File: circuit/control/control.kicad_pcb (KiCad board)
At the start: 2 copper layers, 34 parts, among them J1 Conn_01x02_Socket, J2 Conn_02x20_Row_Letter_Last, J3 Conn_02x20_Row_Letter_Last, Q1 2SC1815, Q2 2SC1815, Q3 2SC1815, Q4 2SC1815, Q5 2SC1815, SW1 SW_Push, U1 ESP32-DevKitC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

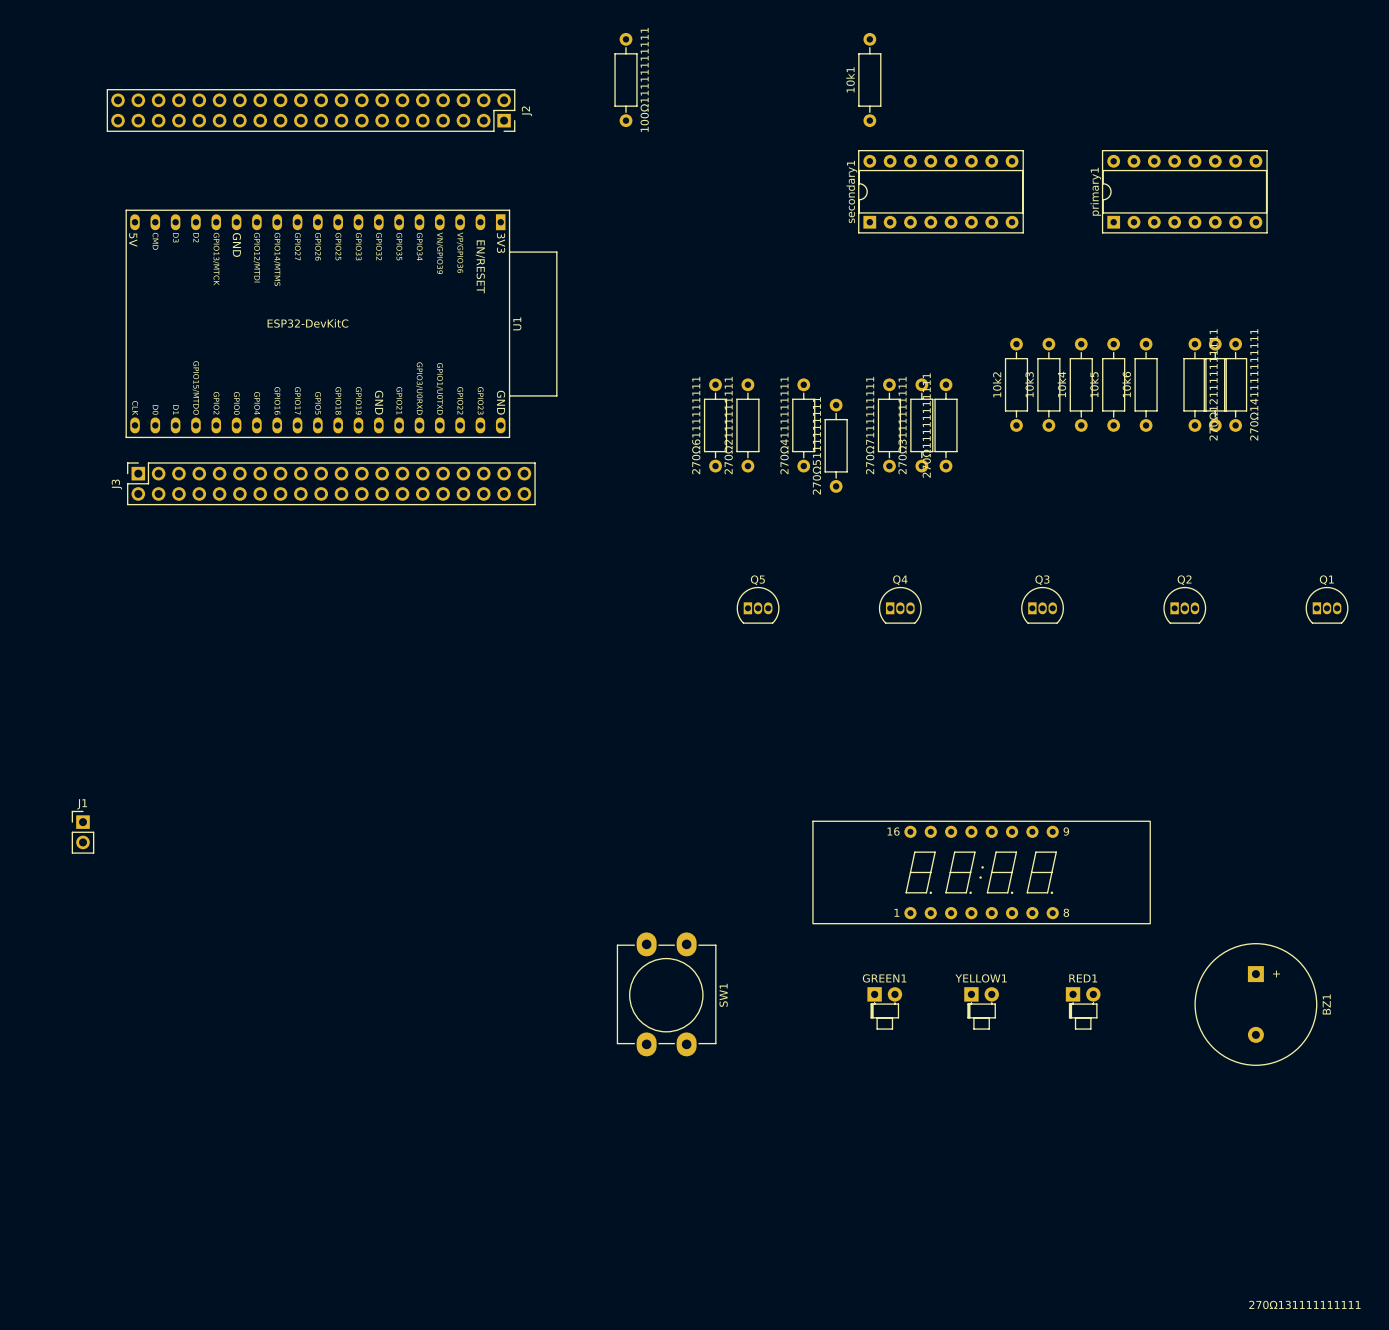
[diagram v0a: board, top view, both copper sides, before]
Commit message: [update] update control circuit
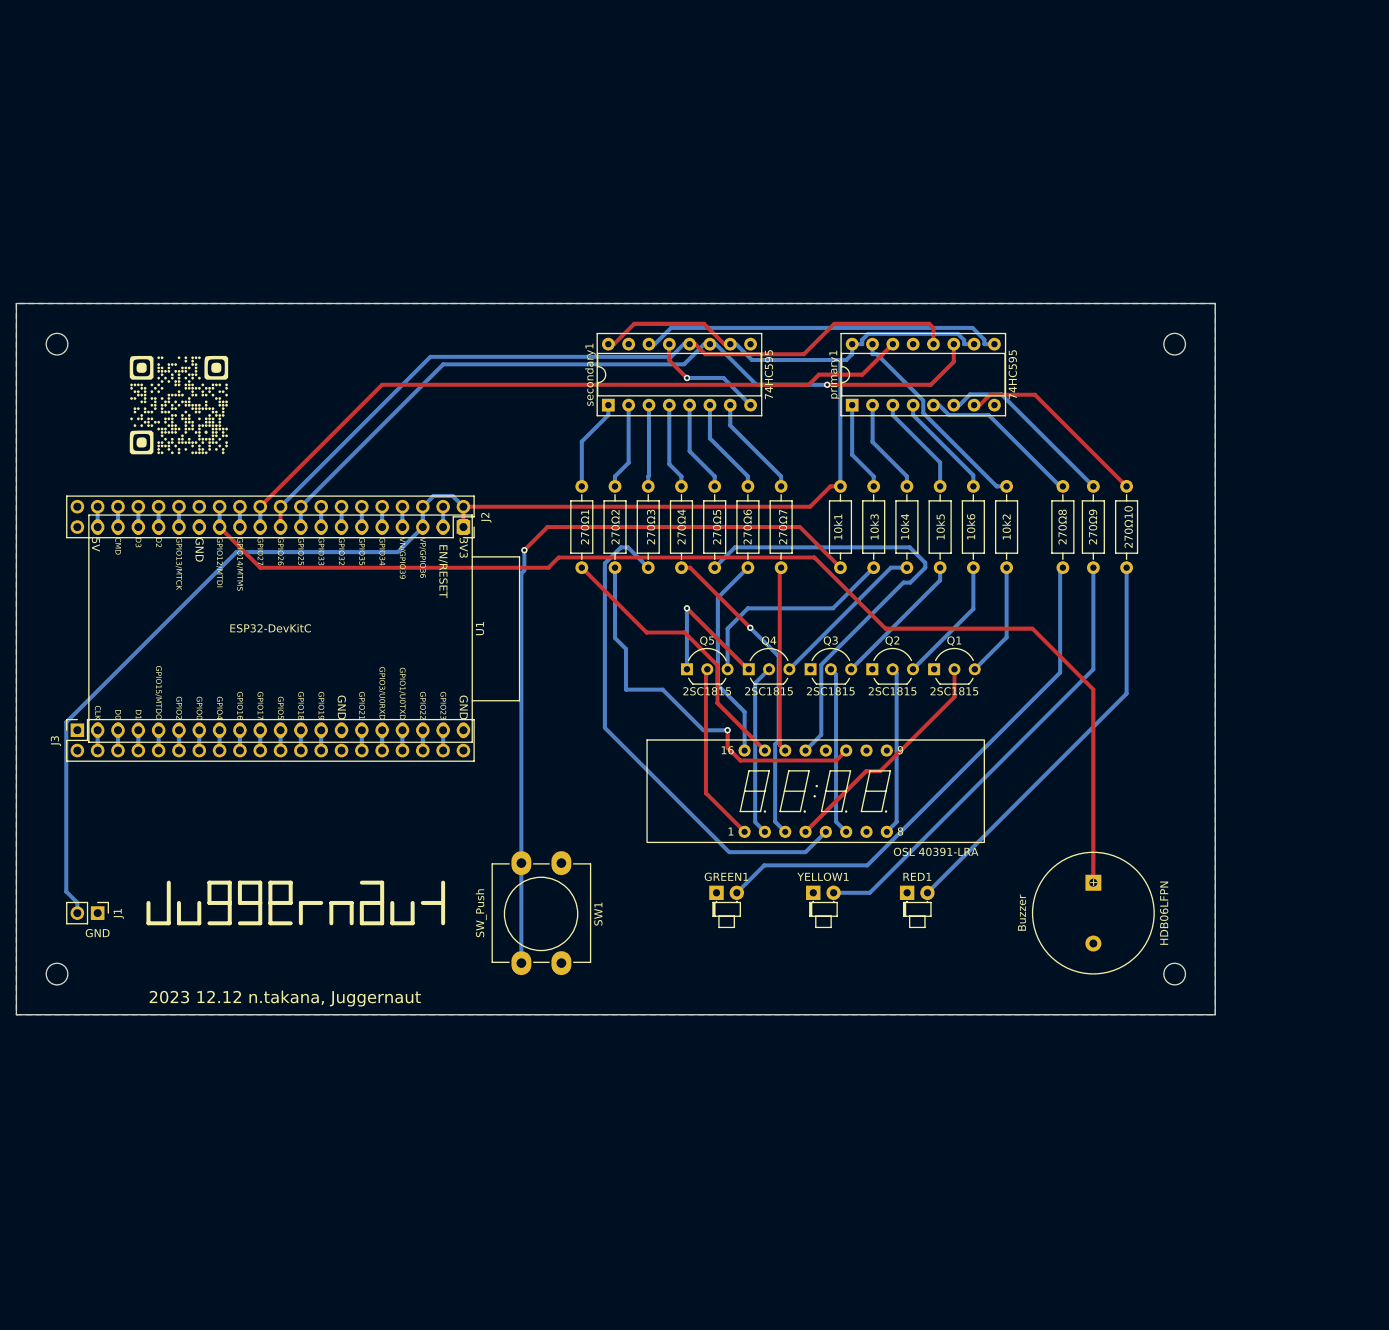
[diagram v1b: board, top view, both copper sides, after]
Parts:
- removed 100Ω11111111111, 270Ω11111111111, 270Ω121111111111, 270Ω131111111111, 270Ω141111111111, 270Ω2111111111, 270Ω3111111111, 270Ω4111111111, 270Ω5111111111, 270Ω6111111111, 270Ω7111111111: R_US, Resistor_THT:R_Axial_DIN0207_L6.3mm_D2.5mm_P10.16mm_Horizontal
- removed BZ1: Buzzer, Buzzer_Beeper:Buzzer_15x7.5RM7.6
- added 270Ω1: R_US, Resistor_THT:R_Axial_DIN0207_L6.3mm_D2.5mm_P10.16mm_Horizontal, F.Cu at (162.1, 96.5)
- added 270Ω10: R_US, Resistor_THT:R_Axial_DIN0207_L6.3mm_D2.5mm_P10.16mm_Horizontal, F.Cu at (230.2, 86.4)
- added 270Ω2: R_US, Resistor_THT:R_Axial_DIN0207_L6.3mm_D2.5mm_P10.16mm_Horizontal, F.Cu at (166.3, 96.5)
- added 270Ω3: R_US, Resistor_THT:R_Axial_DIN0207_L6.3mm_D2.5mm_P10.16mm_Horizontal, F.Cu at (170.4, 96.5)
- added 270Ω4: R_US, Resistor_THT:R_Axial_DIN0207_L6.3mm_D2.5mm_P10.16mm_Horizontal, F.Cu at (174.6, 96.5)
- added 270Ω5: R_US, Resistor_THT:R_Axial_DIN0207_L6.3mm_D2.5mm_P10.16mm_Horizontal, F.Cu at (178.7, 96.5)
- added 270Ω6: R_US, Resistor_THT:R_Axial_DIN0207_L6.3mm_D2.5mm_P10.16mm_Horizontal, F.Cu at (182.9, 96.5)
- added 270Ω7: R_US, Resistor_THT:R_Axial_DIN0207_L6.3mm_D2.5mm_P10.16mm_Horizontal, F.Cu at (187.0, 96.5)
- added 270Ω8: R_US, Resistor_THT:R_Axial_DIN0207_L6.3mm_D2.5mm_P10.16mm_Horizontal, F.Cu at (222.2, 86.4)
- added 270Ω9: R_US, Resistor_THT:R_Axial_DIN0207_L6.3mm_D2.5mm_P10.16mm_Horizontal, F.Cu at (226.1, 86.4)
- added G***: LOGO, Library:QR_juggernaut, F.Cu at (111.8, 76.2)
- added HDB06LFPN: Buzzer, Buzzer_Beeper:Buzzer_15x7.5RM7.6, F.Cu at (226.1, 135.9)
- added hole_lower_left: MountingHole_2.7mm_M2.5, MountingHole:MountingHole_2.7mm_M2.5, F.Cu at (96.5, 147.3)
- added hole_lower_right: MountingHole_2.7mm_M2.5, MountingHole:MountingHole_2.7mm_M2.5, F.Cu at (236.2, 147.3)
- added hole_upper_left: MountingHole_2.7mm_M2.5, MountingHole:MountingHole_2.7mm_M2.5, F.Cu at (96.5, 68.6)
- added hole_upper_right: MountingHole_2.7mm_M2.5, MountingHole:MountingHole_2.7mm_M2.5, F.Cu at (236.2, 68.6)
- Q1, Q2, Q3, Q4, Q5: footprint Package_TO_SOT_THT:TO-92_Inline -> Package_TO_SOT_THT:TO-92_Inline_Wide
- U2: value 4digit_7seg_led -> OSL 40391-LRA
- moved 10k1 56.0 mm to (194.4, 96.5)
- moved J2 51.1 mm to (147.3, 91.4)
- moved Q1 48.4 mm to (206.2, 109.2)
- moved primary1 39.9 mm to (195.9, 76.2)
- moved secondary1 39.9 mm to (165.4, 76.2)
- moved Q2 38.5 mm to (198.4, 109.2)
- moved U1 38.4 mm to (147.3, 91.4)
- moved J3 33.0 mm to (99.1, 116.8)
- moved Q3 28.8 mm to (190.7, 109.2)
- moved 10k3 28.2 mm to (198.6, 96.5)
- moved 10k4 28.1 mm to (202.8, 96.5)
- moved 10k5 28.0 mm to (206.9, 96.5)
- moved 10k6 28.0 mm to (211.1, 96.5)
- moved RED1 24.3 mm to (202.8, 137.2)
- moved GREEN1 23.5 mm to (179.0, 137.2)
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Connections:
- 10k1 pad 1: +3V3 -> Net-(10k1-Pad1)
- J3 pad 32a: unconnected-(J3-Pin_32a-Pad32a) -> GNDPWR
- J3 pad 32b: unconnected-(J3-Pin_32b-Pad32b) -> GNDPWR
- J3 pad 38a: unconnected-(J3-Pin_38a-Pad38a) -> GNDPWR
- J3 pad 38b: unconnected-(J3-Pin_38b-Pad38b) -> GNDPWR
- SW1 pad 2: +3V3 -> Net-(10k1-Pad1)
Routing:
- net +3V3: track 0.00 -> 206.2 mm
- net Net-(BZ1--): track 0.00 -> 145.4 mm
- net Net-(J2-Pin_9a): track 0.00 -> 98.1 mm, vias 0 -> 1
- net Net-(J2-Pin_10a): track 0.00 -> 96.9 mm
- net Net-(10k1-Pad1): track 0.00 -> 94.6 mm, vias 0 -> 1
- net Net-(J2-Pin_11a): track 0.00 -> 90.0 mm
- net Net-(GREEN1-A): track 0.00 -> 64.9 mm
- net Net-(U2-e): track 0.00 -> 63.0 mm
- net Net-(U2-c/D3): track 0.00 -> 58.4 mm
- net Net-(YELLOW1-A): track 0.00 -> 56.7 mm
- net Net-(RED1-A): track 0.00 -> 50.9 mm
- net Net-(U2-f): track 0.00 -> 48.8 mm, vias 0 -> 1
- net Net-(primary1-QH'): track 0.00 -> 45.2 mm
- net Net-(U2-d): track 0.00 -> 39.4 mm, vias 0 -> 1
- net Net-(U2-g): track 0.00 -> 35.1 mm
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- added copper zone on B.Cu, net GNDPWR
- added copper zone on F.Cu, net GNDPWR
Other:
- board outline added: 149.9 x 88.9 mm
- board text added: "2023 12.12 n.takana, Juggernaut"
- board text added: "GND"

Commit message: [update] update control
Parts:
- U2: value OSL 40391-LRA -> 4digit_7seg_led
- renumbered HDB06LFPN to BZ1
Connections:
- 10k1 pad 1: Net-(10k1-Pad1) -> Net-(J2-Pin_3a)
- J2 pad 3a: +3V3 -> Net-(J2-Pin_3a)
- J2 pad 3b: +3V3 -> Net-(J2-Pin_3a)
- SW1 pad 2: Net-(10k1-Pad1) -> Net-(J2-Pin_3a)
- U1 pad 3: +3V3 -> Net-(J2-Pin_3a)
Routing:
- net +3V3: track 206.2 -> 0.00 mm
- net Net-(BZ1--): track 145.4 -> 0.00 mm
- net Net-(J2-Pin_9a): track 98.1 -> 0.00 mm, vias 1 -> 0
- net Net-(J2-Pin_10a): track 96.9 -> 0.00 mm
- net Net-(10k1-Pad1): track 94.6 -> 0.00 mm, vias 1 -> 0
- net Net-(J2-Pin_11a): track 90.0 -> 0.00 mm
- net Net-(GREEN1-A): track 64.9 -> 0.00 mm
- net Net-(U2-e): track 63.0 -> 0.00 mm
- net Net-(U2-c/D3): track 58.4 -> 0.00 mm
- net Net-(YELLOW1-A): track 56.7 -> 0.00 mm
- net Net-(RED1-A): track 50.9 -> 0.00 mm
- net Net-(U2-f): track 48.8 -> 0.00 mm, vias 1 -> 0
- net Net-(primary1-QH'): track 45.2 -> 0.00 mm
- net Net-(U2-d): track 39.4 -> 0.00 mm, vias 1 -> 0
- net Net-(U2-g): track 35.1 -> 0.00 mm
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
